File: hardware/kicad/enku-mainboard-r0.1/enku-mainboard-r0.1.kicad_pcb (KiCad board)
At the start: 4 copper layers, 54 x 94 mm, 156 parts, among them J1 1S LiPo + NTC, J2 Hirose DM3AT-SF-PEJM5, J3 FH34SRJ-24S-0.5SH(50), J4 FH34SRJ-6S-0.5SH(50), J5 GCT USB4105-GF-A-120, J6 4-pin pogo dock, J7 Tag-Connect TC2030-IDC-NL, J8 Pro Wireless Qi raw interface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, Q1 IRLML6346TRPBF, Q2 BSS138LT1G, Q3 BSS138LT1G, SW1 HARD POWER, SW2 BOOT / RECOVERY, SW3 BTN_PREV, SW4 BTN_NEXT, SW5 BTN_SELECT, SW6 BTN_BACK, U1 ESP32-S3-WROOM-1-N16R8, U2 TPS2121, U3 BQ25185DLHR, U4 TPS63802DLAR, U5 BMI270, U6 DRV5032FBDBZR, U7 TPS923610DRLR, U8 USBLC6-2SC6

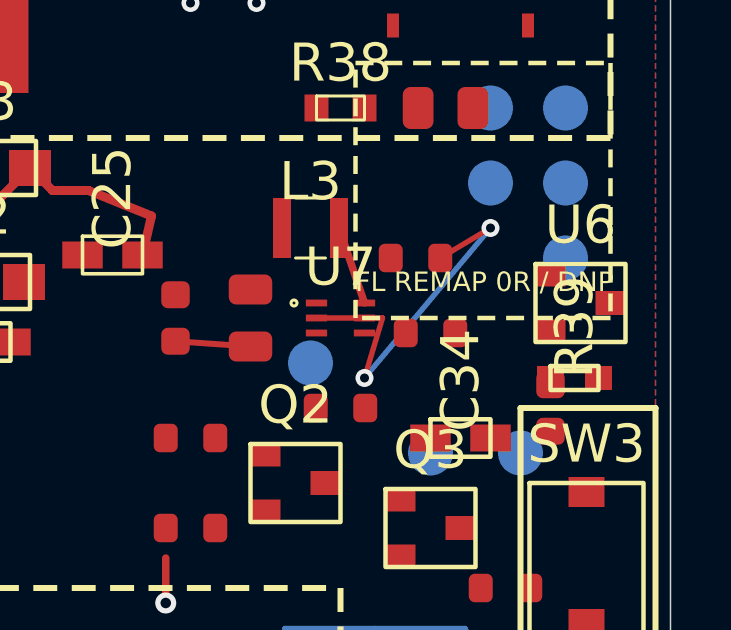
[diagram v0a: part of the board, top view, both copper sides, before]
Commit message: pcb: push ADIM clear of EPD and frontlight pads
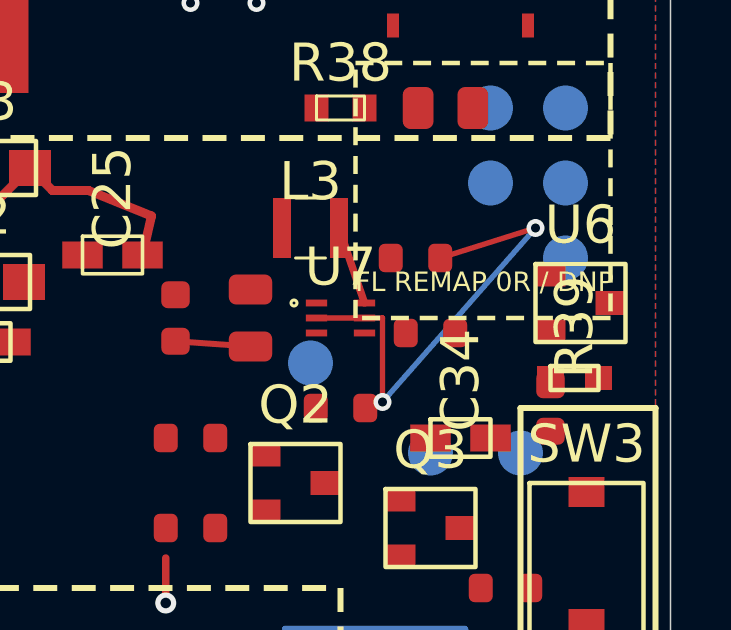
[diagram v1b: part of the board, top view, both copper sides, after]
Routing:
- net FL_ADIM: track 12.8 -> 16.1 mm
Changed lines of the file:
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@@
   (segment (start 62.1999 45.0) (end 64.4 45.0) (width 0.18) (layer "F.Cu") (net 33))
   (segment (start 63.8001 44.5) (end 62.95 42.0) (width 0.25) (layer "F.Cu") (net 36))
-  (segment (start 64.4 45.0) (end 63.8 47.0) (width 0.18) (layer "F.Cu") (net 33))
-  (via (at 63.8 47.0) (size 0.60) (drill 0.30) (layers "F.Cu" "B.Cu") (net 33))
-  (segment (start 63.8 47.0) (end 68.0 42.0) (width 0.18) (layer "B.Cu") (net 33))
-  (via (at 68.0 42.0) (size 0.60) (drill 0.30) (layers "F.Cu" "B.Cu") (net 33))
-  (segment (start 68.0 42.0) (end 66.325 43.0) (width 0.18) (layer "F.Cu") (net 33))
+  (segment (start 64.4 45.0) (end 64.4 47.8) (width 0.18) (layer "F.Cu") (net 33))
+  (via (at 64.4 47.8) (size 0.60) (drill 0.30) (layers "F.Cu" "B.Cu") (net 33))
+  (segment (start 64.4 47.8) (end 69.5 42.0) (width 0.18) (layer "B.Cu") (net 33))
+  (via (at 69.5 42.0) (size 0.60) (drill 0.30) (layers "F.Cu" "B.Cu") (net 33))
+  (segment (start 69.5 42.0) (end 66.325 43.0) (width 0.18) (layer "F.Cu") (net 33))
 )

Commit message: pcb: keep only DRC-safe local frontlight escape
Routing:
- net FL_ADIM: track 16.1 -> 2.20 mm, vias 2 -> 0
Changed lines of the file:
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@@
   (segment (start 62.1999 45.0) (end 64.4 45.0) (width 0.18) (layer "F.Cu") (net 33))
   (segment (start 63.8001 44.5) (end 62.95 42.0) (width 0.25) (layer "F.Cu") (net 36))
-  (segment (start 64.4 45.0) (end 64.4 47.8) (width 0.18) (layer "F.Cu") (net 33))
-  (via (at 64.4 47.8) (size 0.60) (drill 0.30) (layers "F.Cu" "B.Cu") (net 33))
-  (segment (start 64.4 47.8) (end 69.5 42.0) (width 0.18) (layer "B.Cu") (net 33))
-  (via (at 69.5 42.0) (size 0.60) (drill 0.30) (layers "F.Cu" "B.Cu") (net 33))
-  (segment (start 69.5 42.0) (end 66.325 43.0) (width 0.18) (layer "F.Cu") (net 33))
 )

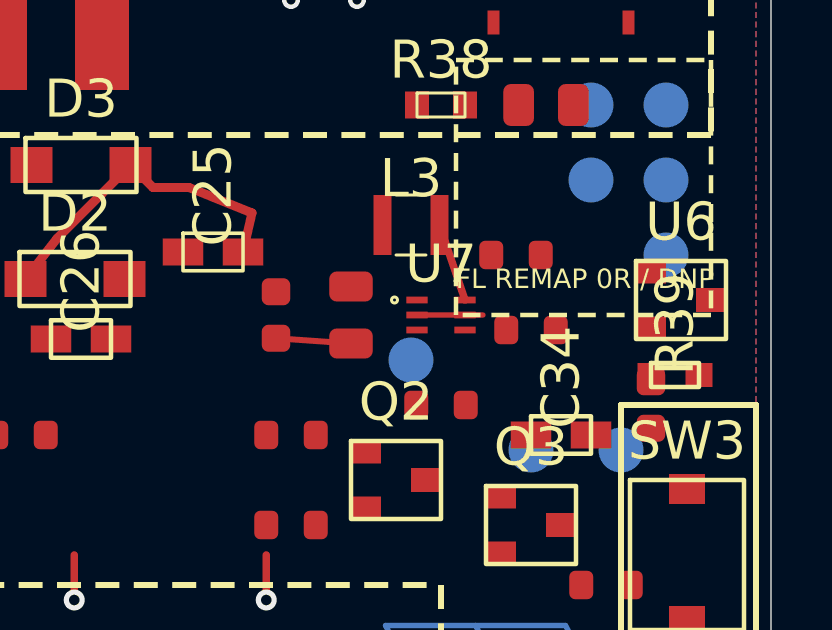
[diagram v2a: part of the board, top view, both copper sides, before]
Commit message: pcb: drop ADIM partial escape pending placement rework
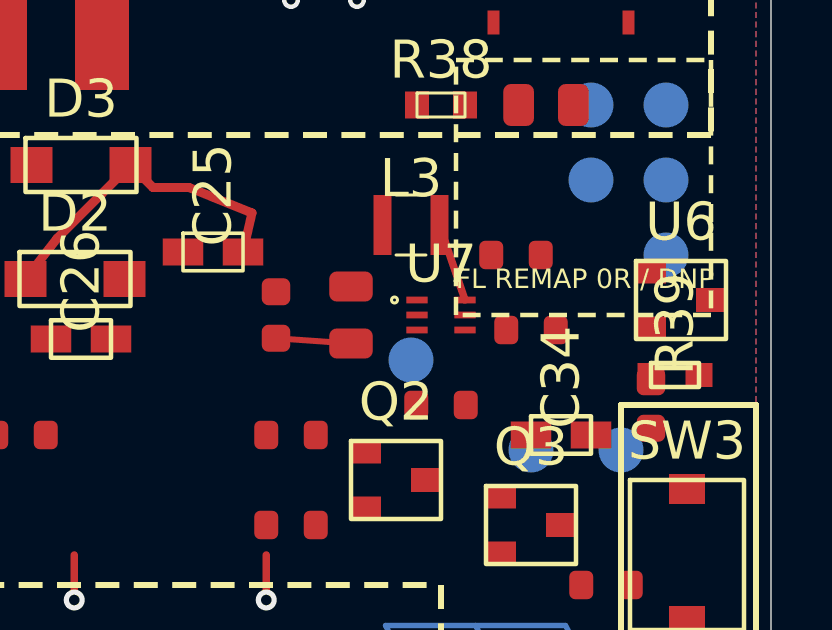
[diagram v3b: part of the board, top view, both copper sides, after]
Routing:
- net FL_ADIM: track 2.20 -> 0.00 mm
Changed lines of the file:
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@@
   (segment (start 58 34.5) (end 58 32.95) (width 0.18) (layer "F.Cu") (net 15))
   (segment (start 29.200 55.000) (end 30.000 55.000) (width 0.25) (layer "F.Cu") (net 2))
-  (segment (start 62.1999 45.0) (end 64.4 45.0) (width 0.18) (layer "F.Cu") (net 33))
   (segment (start 63.8001 44.5) (end 62.95 42.0) (width 0.25) (layer "F.Cu") (net 36))
 )

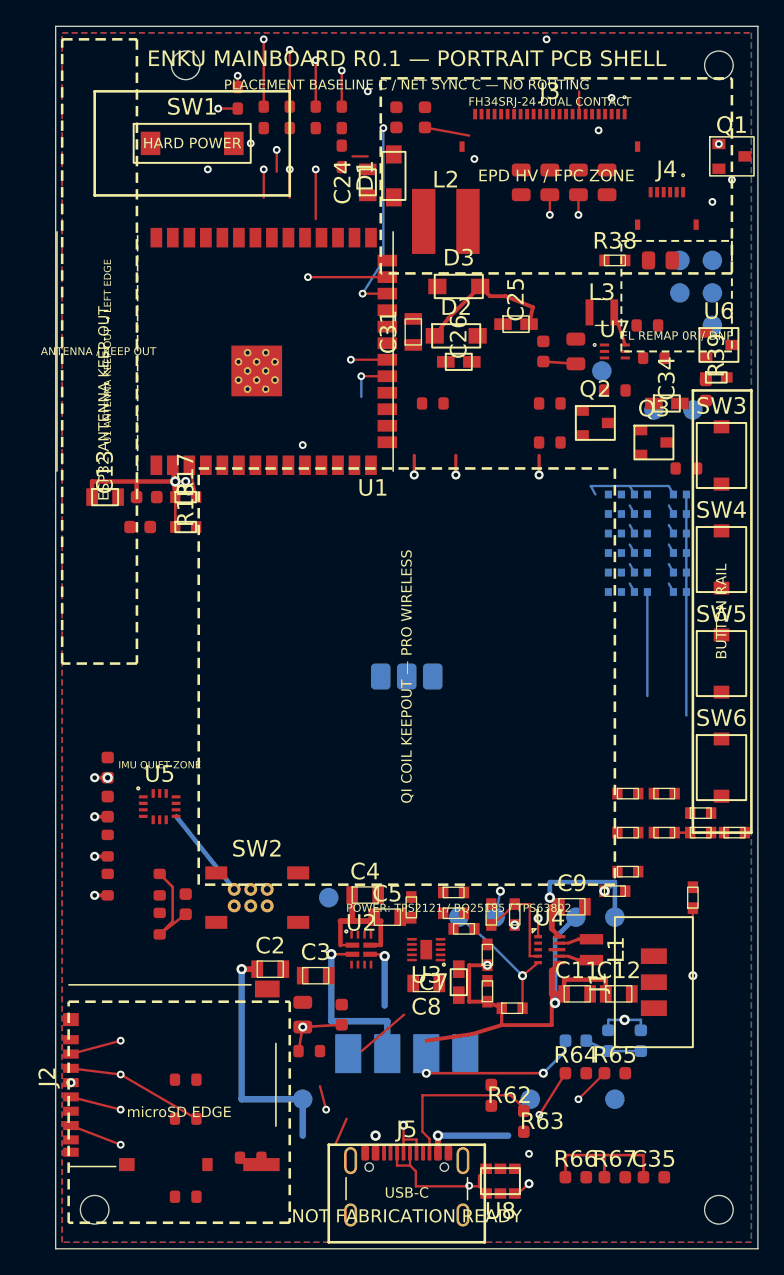
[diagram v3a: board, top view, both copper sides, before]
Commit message: pcb: eliminate residual pad shorts and ESP enable clearance
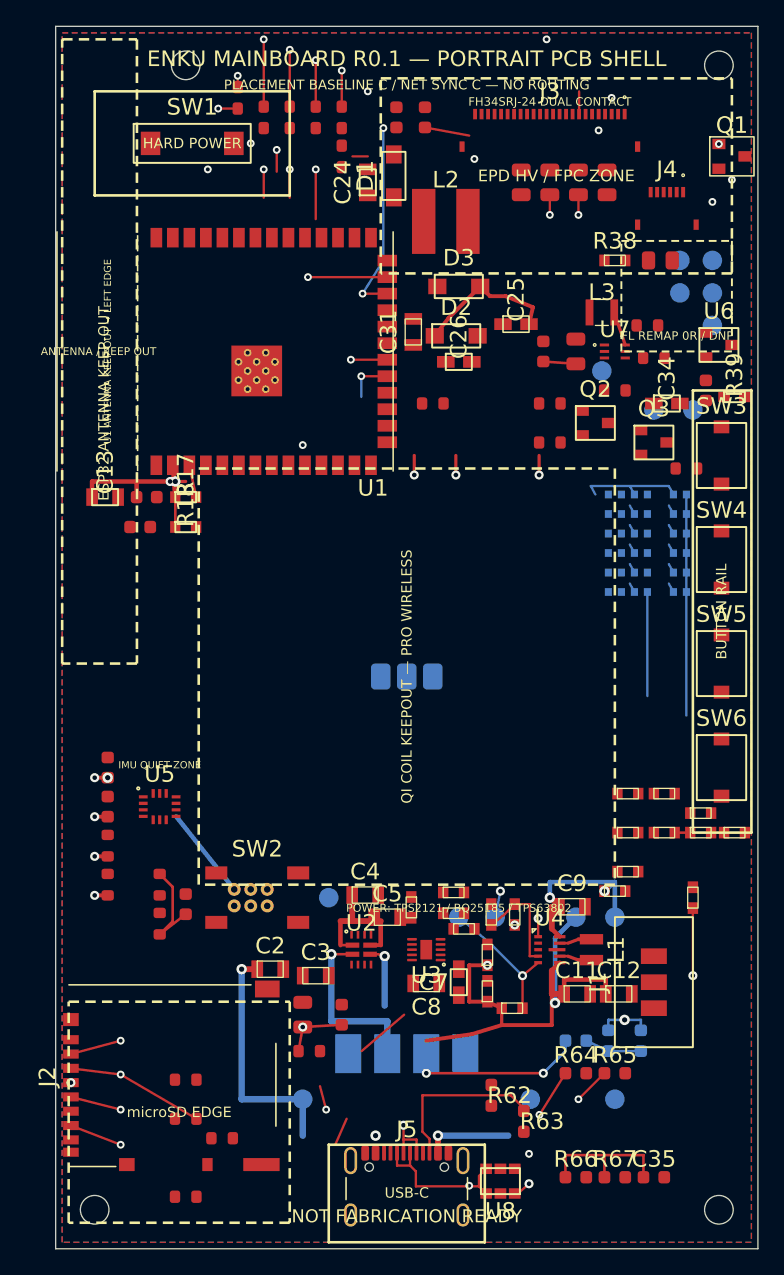
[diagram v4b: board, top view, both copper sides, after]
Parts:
- moved R21 2.66 mm to (32.8, 105.5)
- moved R39 2.05 mm to (72.2, 48.5)
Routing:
- net 3V3_SYS: track 194.5 -> 195.7 mm
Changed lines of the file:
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@@
   )
   (footprint "Resistor_SMD:R_0603_1608Metric" (layer "F.Cu")
-    (at 70.8 47 0)
+    (at 72.2 48.5 0)
     (property "Reference" "R39" (at 0 -1.7000000000000002 90) (layer "F.SilkS"))
     (property "Value" "15R 1%" (at 0 1.7000000000000002 90) (layer "F.Fab") hide)
@@
   )
   (footprint "Resistor_SMD:R_0603_1608Metric" (layer "F.Cu")
-    (at 35 107)
+    (at 32.8 105.5)
     (property "Reference" "R21" (at 0 -1.5 0) (layer "F.SilkS") hide)
     (property "Value" "0R (22R tune)" (at 0 1.5 0) (layer "F.Fab") hide)
@@
   (segment (start 23.000 86.825) (end 21.175 101.225) (width 0.30) (layer "In2.Cu") (net 2))
   (via (at 21.175 101.225) (size 0.70) (drill 0.35) (layers "F.Cu" "In2.Cu") (net 2))
-  (via (at 30.000 55.000) (size 0.70) (drill 0.35) (layers "F.Cu" "In2.Cu") (net 2))
-  (segment (start 30.000 55.000) (end 47.575 54.500) (width 0.25) (layer "In2.Cu") (net 2))
+  (via (at 28.800 55.000) (size 0.70) (drill 0.35) (layers "F.Cu" "In2.Cu") (net 2))
+  (segment (start 28.800 55.000) (end 47.575 54.500) (width 0.25) (layer "In2.Cu") (net 2))
   (segment (start 61.500 56.000) (end 61.150 55.350) (width 0.18) (layer "B.Cu") (net 37))
   (segment (start 64.500 56.000) (end 64.150 55.350) (width 0.18) (layer "B.Cu") (net 37))

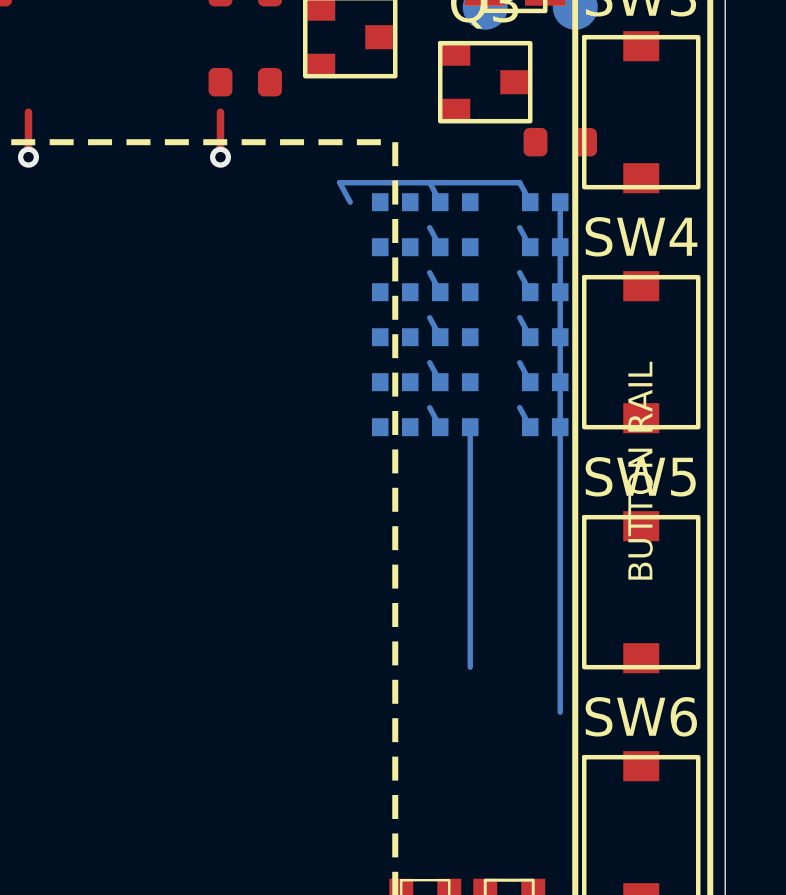
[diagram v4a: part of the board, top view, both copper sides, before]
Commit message: pcb: purge obsolete frontlight raw routing tails
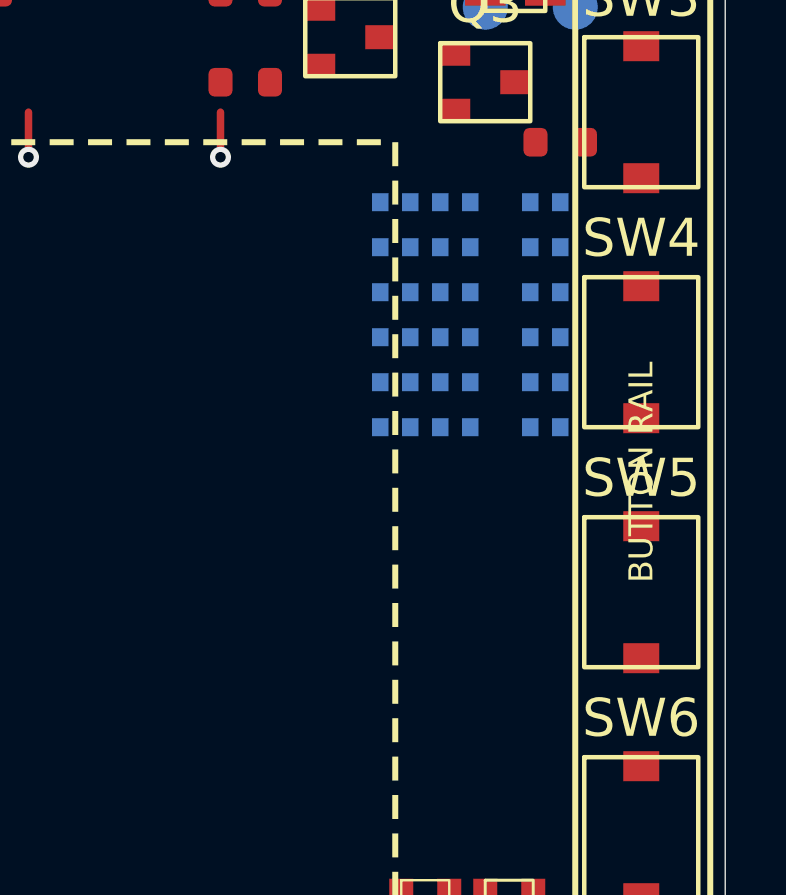
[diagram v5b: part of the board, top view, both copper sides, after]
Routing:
- net FL_COOL_RETURN: track 17.0 -> 0.00 mm
- net FL_RAW1: track 8.21 -> 0.00 mm
- net FL_WARM_RETURN: track 8.00 -> 0.00 mm
- net FL_RAW6: track 1.48 -> 0.00 mm
- net FL_RAW5: track 1.48 -> 0.00 mm
- net FL_RAW4: track 1.48 -> 0.00 mm
- net FL_RAW3: track 1.48 -> 0.00 mm
- net FL_RAW2: track 1.48 -> 0.00 mm
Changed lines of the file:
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@@
   (via (at 28.800 55.000) (size 0.70) (drill 0.35) (layers "F.Cu" "In2.Cu") (net 2))
   (segment (start 28.800 55.000) (end 47.575 54.500) (width 0.25) (layer "In2.Cu") (net 2))
-  (segment (start 61.500 56.000) (end 61.150 55.350) (width 0.18) (layer "B.Cu") (net 37))
-  (segment (start 64.500 56.000) (end 64.150 55.350) (width 0.18) (layer "B.Cu") (net 37))
-  (segment (start 67.500 56.000) (end 67.150 55.350) (width 0.18) (layer "B.Cu") (net 37))
-  (segment (start 61.150 55.350) (end 67.150 55.350) (width 0.18) (layer "B.Cu") (net 37))
-  (segment (start 64.500 57.500) (end 64.150 56.850) (width 0.18) (layer "B.Cu") (net 38))
-  (segment (start 67.500 57.500) (end 67.150 56.850) (width 0.18) (layer "B.Cu") (net 38))
-  (segment (start 64.500 59.000) (end 64.150 58.350) (width 0.18) (layer "B.Cu") (net 39))
-  (segment (start 67.500 59.000) (end 67.150 58.350) (width 0.18) (layer "B.Cu") (net 39))
-  (segment (start 64.500 60.500) (end 64.150 59.850) (width 0.18) (layer "B.Cu") (net 40))
-  (segment (start 67.500 60.500) (end 67.150 59.850) (width 0.18) (layer "B.Cu") (net 40))
-  (segment (start 64.500 62.000) (end 64.150 61.350) (width 0.18) (layer "B.Cu") (net 41))
-  (segment (start 67.500 62.000) (end 67.150 61.350) (width 0.18) (layer "B.Cu") (net 41))
-  (segment (start 64.500 63.500) (end 64.150 62.850) (width 0.18) (layer "B.Cu") (net 42))
-  (segment (start 67.500 63.500) (end 67.150 62.850) (width 0.18) (layer "B.Cu") (net 42))
-  (segment (start 68.500 56.000) (end 68.500 63.500) (width 0.18) (layer "B.Cu") (net 46))
-  (segment (start 65.500 63.500) (end 65.500 71.500) (width 0.18) (layer "B.Cu") (net 44))
-  (segment (start 68.500 63.500) (end 68.500 73.000) (width 0.18) (layer "B.Cu") (net 46))
   (segment (start 60.25 26.750) (end 60.25 25.000) (width 0.18) (layer "F.Cu") (net 16))
   (segment (start 60.25 25.000) (end 40 25.000) (width 0.18) (layer "In1.Cu") (net 16))

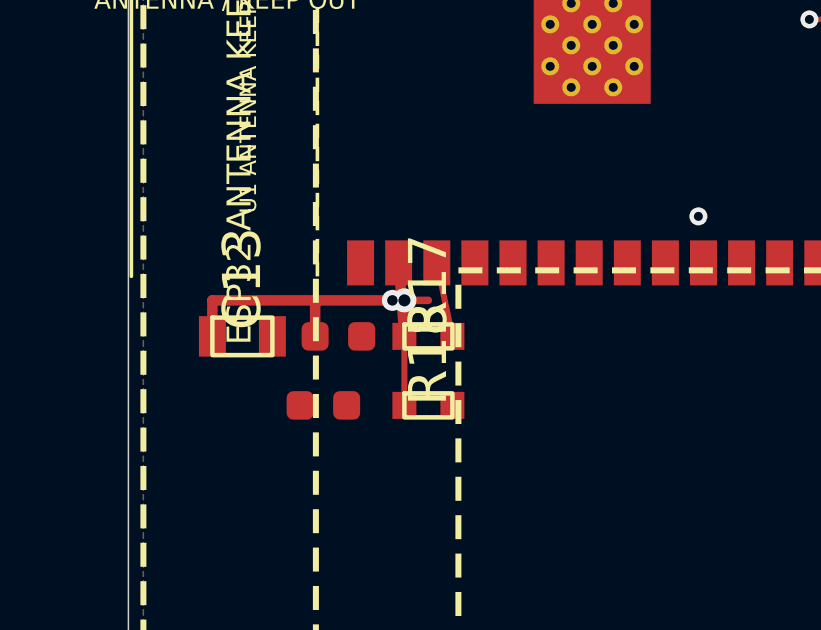
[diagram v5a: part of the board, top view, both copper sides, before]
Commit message: pcb: remove obsolete duplicate 3V3 via stub
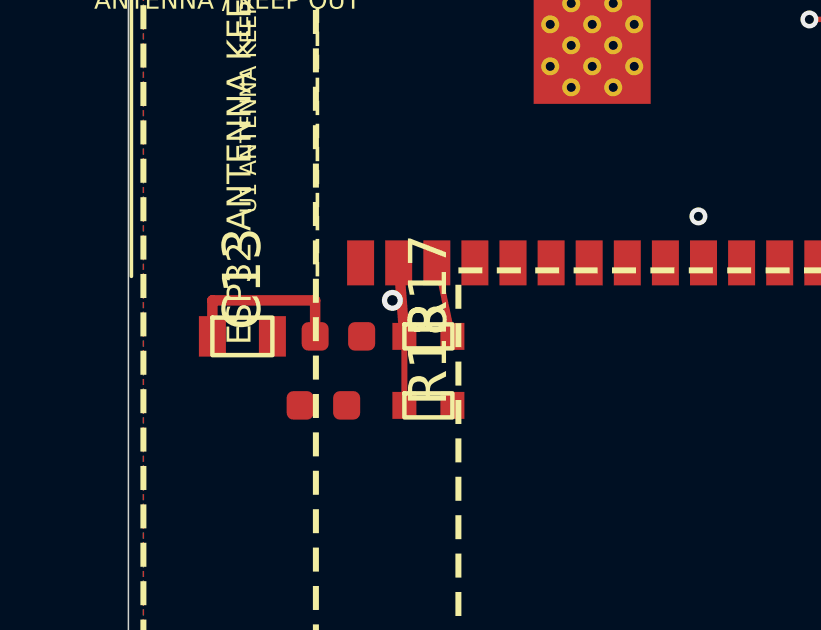
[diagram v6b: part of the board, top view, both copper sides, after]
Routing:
- net 3V3_SYS: track 195.7 -> 167.4 mm, vias 15 -> 14
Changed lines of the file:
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@@
   (segment (start 22.800 55.000) (end 26.225 55.000) (width 0.35) (layer "F.Cu") (net 2))
   (segment (start 26.225 55.000) (end 26.225 56.200) (width 0.35) (layer "F.Cu") (net 2))
-  (segment (start 26.225 55.000) (end 29.200 55.000) (width 0.35) (layer "F.Cu") (net 2))
-  (segment (start 29.200 55.000) (end 29.200 56.200) (width 0.35) (layer "F.Cu") (net 2))
   (segment (start 29.200 56.200) (end 29.010 53.750) (width 0.35) (layer "F.Cu") (net 2))
-  (via (at 29.200 55.000) (size 0.80) (drill 0.40) (layers "F.Cu" "In1.Cu") (net 2))
-  (segment (start 29.200 55.000) (end 24.000 77.775) (width 0.35) (layer "In1.Cu") (net 2))
   (via (at 24.000 77.775) (size 0.80) (drill 0.40) (layers "F.Cu" "In1.Cu") (net 2))
   (segment (start 24.000 77.775) (end 23.000 77.775) (width 0.30) (layer "F.Cu") (net 2))
@@
   (via (at 58 34.5) (size 0.60) (drill 0.30) (layers "F.Cu" "In2.Cu") (net 15))
   (segment (start 58 34.5) (end 58 32.95) (width 0.18) (layer "F.Cu") (net 15))
-  (segment (start 29.200 55.000) (end 30.000 55.000) (width 0.25) (layer "F.Cu") (net 2))
   (segment (start 63.8001 44.5) (end 62.95 42.0) (width 0.25) (layer "F.Cu") (net 36))
 )
